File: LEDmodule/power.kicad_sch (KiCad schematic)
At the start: 0 parts

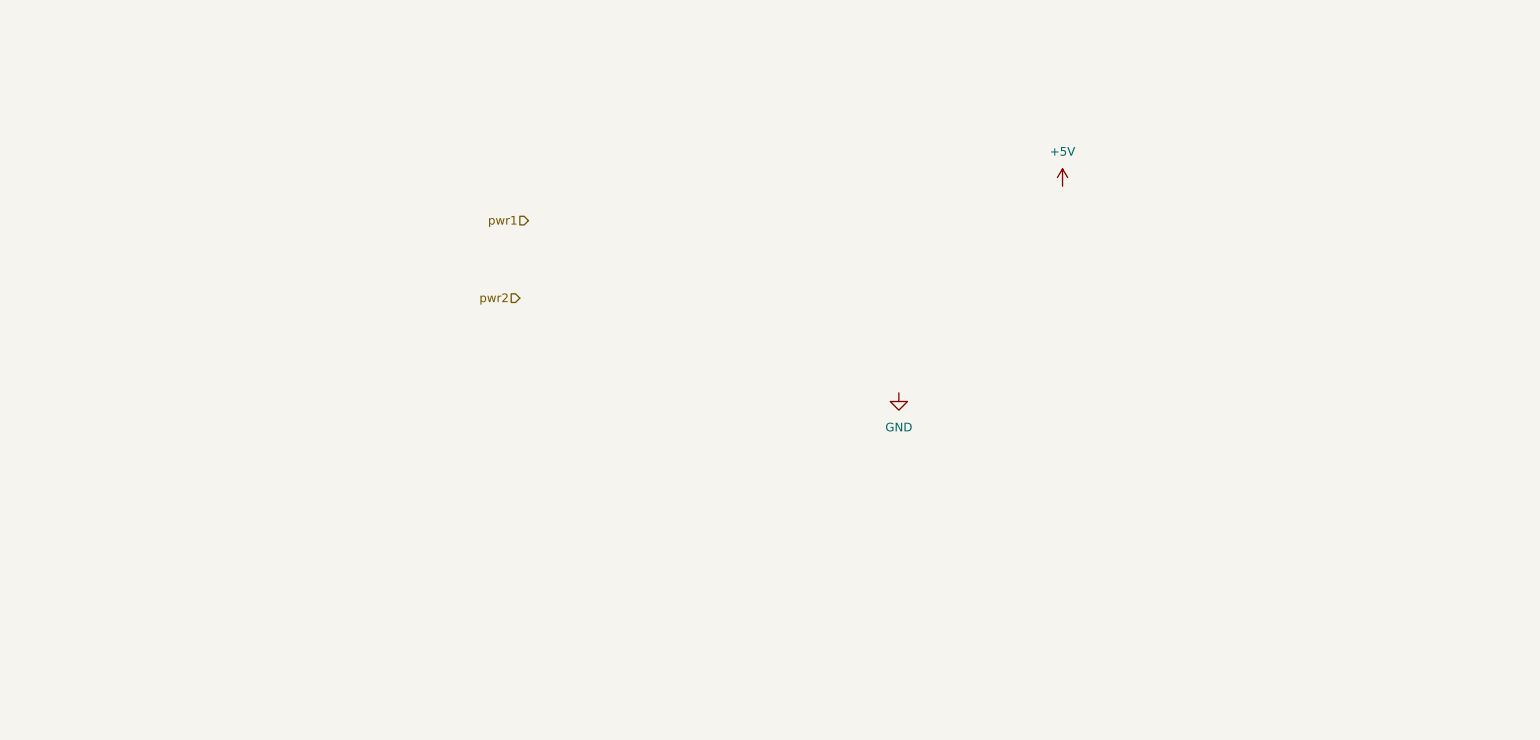
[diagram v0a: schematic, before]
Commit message: Initial buck converter design
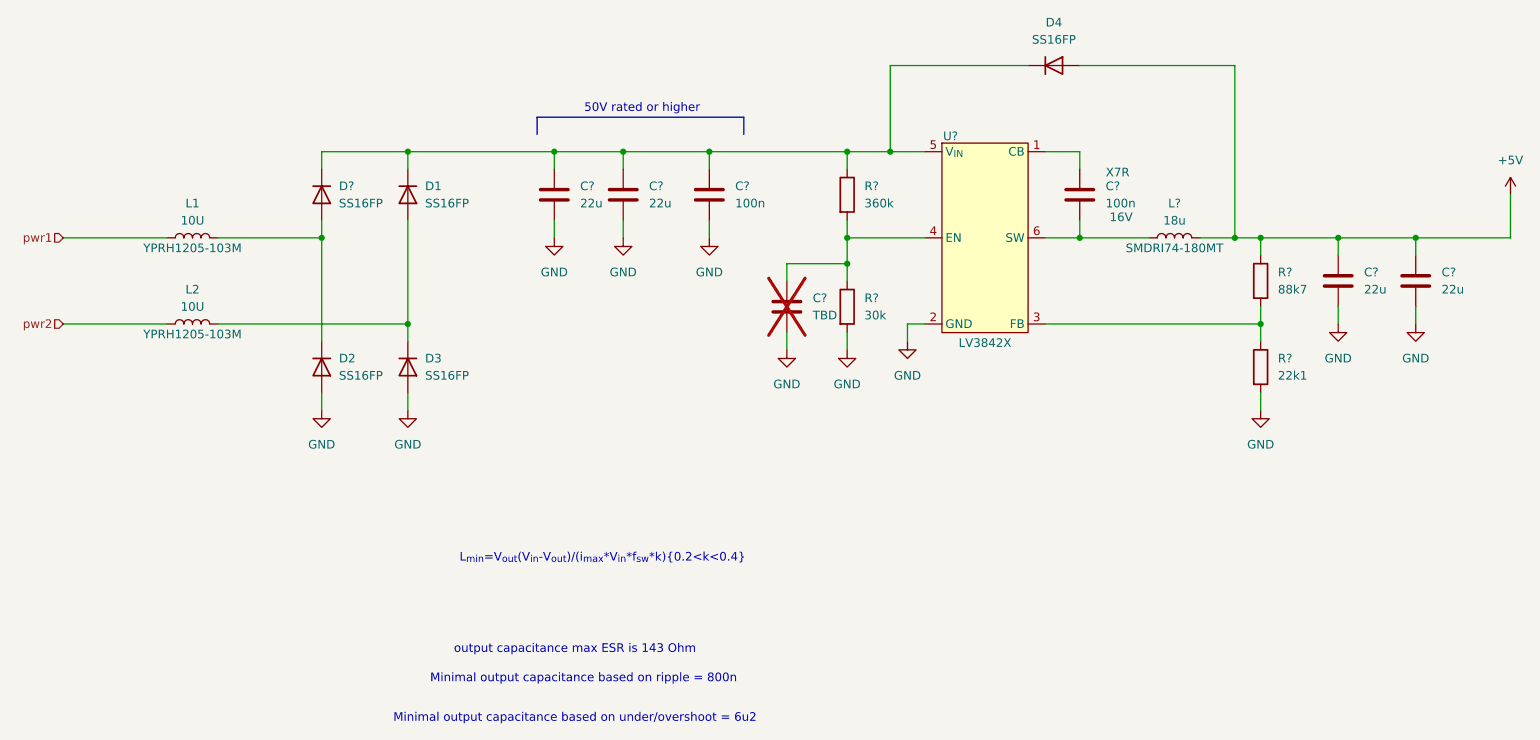
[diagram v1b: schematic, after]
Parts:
- added C? (x4): 22u, symbol Device:C
- added C?: TBD, symbol Device:C
- added C? (x2): 100n, symbol Device:C
- added D1, D2, D3, D4, D?: SS16FP, symbol Device:D
- added L1, L2: 10U, symbol Device:L
- added L?: 18u, symbol Device:L
- added R?: 22k1, symbol Device:R
- added R?: 88k7, symbol Device:R
- added R?: 360k, symbol Device:R
- added R?: 30k, symbol Device:R
- added U?: LV3842X, Package_TO_SOT_SMD:SOT-23-6, symbol LV3842:LV3842X
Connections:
- net +5V: now also C?.1, C?.1, D4.2 (A), L?.2, R?.1
- net GND: now also C?.2, C?.2, C?.2, C?.2, C?.2, C?.2, D2.2 (A), D3.2 (A), R?.2, R?.2, U?.2 (GND)
- net pwr1: now also L1.1
- net pwr2: now also L2.1
- new net: R?.1, R?.2, U?.3 (FB)
- new net: C?.1, C?.1, C?.1, D1.1 (K), D4.1 (K), D?.1 (K), R?.1, U?.5 (V_{IN})
- new net: D1.2 (A), D3.1 (K), L2.2
- new net: C?.1, R?.1, R?.2, U?.4 (EN)
- new net: D2.1 (K), D?.2 (A), L1.2
- new net: C?.2, L?.1, U?.6 (SW)
- new net: C?.1, U?.1 (CB)
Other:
- note added: "50V rated or higher"
- note added: "L_{min}=V_{out}(V_{in}-V_{out})/(i_{max}*V_{in}*f_{sw}*k){0.2<k<0.4}"
- note added: "Minimal output capacitance based on ripple = 800n"
- note added: "Minimal output capacitance based on under/overshoot = 6u2"
- note added: "output capacitance max ESR is 143 Ohm"

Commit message: Add start of comm's
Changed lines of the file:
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@@
 	(text "output capacitance max ESR is 143 Ohm"
 		(exclude_from_sim no)
-		(at 113.538 149.606 0)
+		(at 115.824 145.542 0)
 		(effects
 			(font
@@
 	(text "Minimal output capacitance based on ripple = 800n"
 		(exclude_from_sim no)
-		(at 114.808 153.924 0)
+		(at 117.094 149.86 0)
 		(effects
 			(font
@@
 	(text "Minimal output capacitance based on under/overshoot = 6u2"
 		(exclude_from_sim no)
-		(at 113.538 159.766 0)
+		(at 115.824 155.702 0)
 		(effects
 			(font
